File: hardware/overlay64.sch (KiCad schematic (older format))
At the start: 26 parts, among them P2 MAIN, P3 CONTROL, P6 HOLE, P7 HOLE, P8 HOLE, P9 HOLE, Q1 BC547B, U1 LM1881, Y1 20MHz

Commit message: Hardware: Updated schematics, added BURST signal connection
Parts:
- removed P3: CONTROL, Pin_Headers:Pin_Header_Angled_1x02, symbol CONN_01X02
- added P2: INPUT, symbol CONN_01X16
- added P3: CONTROL, symbol CONN_01X08
- R1, R2, R3: renamed from R?; footprint (none) -> Discret:R1
- gave numbers to parts that had none: 4
- renumbered C3 to C1, C1 to C2, C2 to C3, C5 to C4, C6 to C5, C4 to C6, P2 to P4, P6 to P5, P7 to P6, P8 to P7, P9 to P8, R2 to R4, R1 to R5
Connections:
- net labels added: C0, C1, C2, C3, C4, C5, IN0, IN1, IN10, IN11, IN12, IN13, IN14, IN15, IN2, IN3, IN4, IN5, IN6, IN7, IN8, IN9, ~BURST
- wire segments 25 -> 27
- no-connect marks 30 -> 6
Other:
- moved on the sheet: C1, C5, C6, P5, P6, P7, P8, R5

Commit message: Hardware: Added custom components, started layout
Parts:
- added P9: BYPASS, Pin_Headers:Pin_Header_Angled_1x16, symbol CONN_01X16
- D1, D2: footprint (none) -> custom:Diode-2.5mm-Vertical
- IC1: footprint DIL40 -> Housings_DIP:DIP-40_W15.24mm
- P1: footprint (none) -> custom:USB-MINI-B-TH
- P2: footprint (none) -> Pin_Headers:Pin_Header_Angled_1x16
- P3: footprint (none) -> Pin_Headers:Pin_Header_Angled_1x08
- R1, R2, R3, R4, R5: footprint Discret:R1 -> custom:R1
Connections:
- net C0: now also P3.6 (P6); no longer P3.3 (P3)
- net C1: now also P3.5 (P5); no longer P3.4 (P4)
- net C2: now also P3.4 (P4); no longer P3.5 (P5)
- net C3: now also P3.3 (P3); no longer P3.6 (P6)
- net C4: now also P3.2 (P2); no longer P3.7 (P7)
- net C5: now also P3.1 (P1); no longer P3.8 (P8)
- net D-: now also R3.1; no longer R3.2
- net IN0: now also P2.16 (P16), P9.1 (P1); no longer P2.1 (P1)
- net IN1: now also P2.15 (P15), P9.2 (P2); no longer P2.2 (P2)
- net IN10: now also IC1.27 ((PCINT21/TDI)PC5), P2.6 (P6), P9.11 (P11); no longer IC1.24 ((PCINT18/TCK)PC2), P2.11 (P11)
- net IN11: now also IC1.26 ((PCINT20/TDO)PC4), P2.5 (P5), P9.12 (P12); no longer IC1.25 ((PCINT19/TMS)PC3), P2.12 (P12)
- net IN12: now also IC1.25 ((PCINT19/TMS)PC3), P2.4 (P4), P9.13 (P13); no longer IC1.26 ((PCINT20/TDO)PC4), P2.13 (P13)
- net IN13: now also IC1.24 ((PCINT18/TCK)PC2), P2.3 (P3), P9.14 (P14); no longer IC1.27 ((PCINT21/TDI)PC5), P2.14 (P14)
- net IN14: now also IC1.23 ((PCINT17/SDA)PC1), P2.2 (P2), P9.15 (P15); no longer IC1.28 ((PCINT22/TOSC1)PC6), P2.15 (P15)
- net IN15: now also IC1.22 ((PCINT16/SCL)PC0), P2.1 (P1), P9.16 (P16); no longer IC1.29 ((PCINT23/TOSC2)PC7), P2.16 (P16)
- net IN2: now also P2.14 (P14), P9.3 (P3); no longer P2.3 (P3)
- net IN3: now also P2.13 (P13), P9.4 (P4); no longer P2.4 (P4)
- net IN4: now also P2.12 (P12), P9.5 (P5); no longer P2.5 (P5)
- net IN5: now also P2.11 (P11), P9.6 (P6); no longer P2.6 (P6)
- net IN6: now also P2.10 (P10), P9.7 (P7); no longer P2.7 (P7)
- net IN7: now also P2.9 (P9), P9.8 (P8); no longer P2.8 (P8)
- net IN8: now also IC1.29 ((PCINT23/TOSC2)PC7), P2.8 (P8), P9.9 (P9); no longer IC1.22 ((PCINT16/SCL)PC0), P2.9 (P9)
- net IN9: now also IC1.28 ((PCINT22/TOSC1)PC6), P2.7 (P7), P9.10 (P10); no longer IC1.23 ((PCINT17/SDA)PC1), P2.10 (P10)
- net VCC: now also R3.2; no longer R3.1
- net ~OE: now also P3.8 (P8); no longer P3.1 (P1)
- net ~OR: now also P3.7 (P7); no longer P3.2 (P2)
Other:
- moved on the sheet: P2, P3

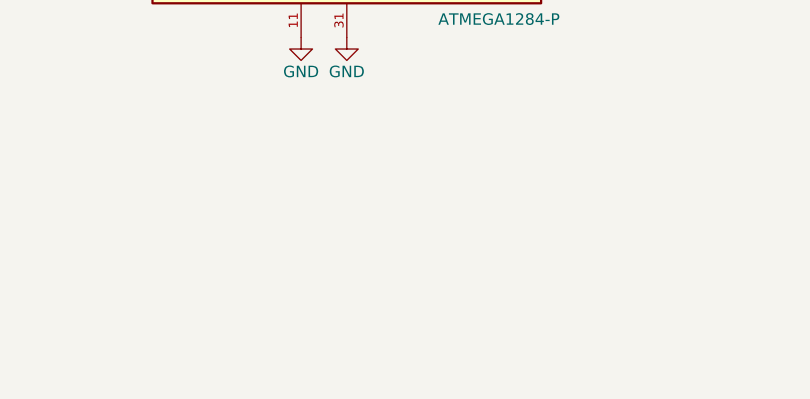
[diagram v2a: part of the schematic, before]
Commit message: Hardware: Added jumpers for manually entering the bootloader
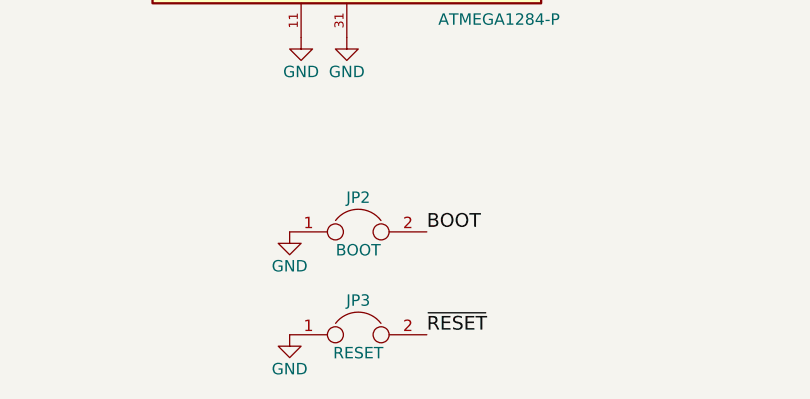
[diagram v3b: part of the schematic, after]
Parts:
- added JP2: BOOT, custom:Pin_Header_Straight_1x02_Pitch2.00mm, symbol JUMPER
- added JP3: RESET, custom:Pin_Header_Straight_1x02_Pitch2.00mm, symbol JUMPER
- JP1: footprint Pin_Headers:Pin_Header_Straight_1x02 -> custom:Pin_Header_Straight_1x02_Pitch2.00mm
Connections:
- net BOOT: now also JP2.2
- net GND: now also JP2.1, JP3.1
- net ~RESET: now also JP3.2
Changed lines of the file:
@@
 F 0 "JP1" H 7300 1750 50  0000 C CNN
 F 1 "BACKDROP" H 7300 1520 50  0000 C CNN
-F 2 "Pin_Headers:Pin_Header_Straight_1x02" H 7300 1600 50  0001 C CNN
+F 2 "custom:Pin_Header_Straight_1x02_Pitch2.00mm" H 7300 1600 50  0001 C CNN
 F 3 "" H 7300 1600 50  0000 C CNN
 	1    7300 1600
@@
 Text Label 8100 4200 0    60   ~ 0
 IN15
+$Comp
+L GND #PWR025
+U 1 1 57B5BB3D
+P 2750 6800
+F 0 "#PWR025" H 2750 6550 50  0001 C CNN
+F 1 "GND" H 2750 6650 50  0000 C CNN
+F 2 "" H 2750 6800 50  0000 C CNN
+F 3 "" H 2750 6800 50  0000 C CNN
+	1    2750 6800
+	1    0    0    -1
+$EndComp
+$Comp
+L GND #PWR026
+U 1 1 57B5BBC8
+P 2750 6350
+F 0 "#PWR026" H 2750 6100 50  0001 C CNN
+F 1 "GND" H 2750 6200 50  0000 C CNN
+F 2 "" H 2750 6350 50  0000 C CNN
+F 3 "" H 2750 6350 50  0000 C CNN
+	1    2750 6350
+	1    0    0    -1
+$EndComp
+Text Label 3350 6350 0    60   ~ 0
+BOOT
+Text Label 3350 6800 0    60   ~ 0
+~RESET
+$Comp
+L JUMPER JP2
+U 1 1 57B5CD17
+P 3050 6350
+F 0 "JP2" H 3050 6500 50  0000 C CNN
+F 1 "BOOT" H 3050 6270 50  0000 C CNN
+F 2 "custom:Pin_Header_Straight_1x02_Pitch2.00mm" H 3050 6350 50  0001 C CNN
+F 3 "" H 3050 6350 50  0000 C CNN
+	1    3050 6350
+	1    0    0    -1
+$EndComp
+$Comp
+L JUMPER JP3
+U 1 1 57B5CDC9
+P 3050 6800
+F 0 "JP3" H 3050 6950 50  0000 C CNN
+F 1 "RESET" H 3050 6720 50  0000 C CNN
+F 2 "custom:Pin_Header_Straight_1x02_Pitch2.00mm" H 3050 6800 50  0001 C CNN
+F 3 "" H 3050 6800 50  0000 C CNN
+	1    3050 6800
+	1    0    0    -1
+$EndComp
 $EndSCHEMATC

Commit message: Hardware: Prototype 2, rearranged, rerouted, added gerber files
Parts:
- D1, D2: footprint custom:Diode-2.5mm-Vertical -> custom:D3
- IC1: value ATMEGA1284-P -> ATMEGA1284
- JP1, JP2, JP3: footprint custom:Pin_Header_Straight_1x02_Pitch2.00mm -> custom:Pin_Header_Straight_1x02
- R1, R2, R3, R4, R5: footprint custom:R1 -> Discret:R3
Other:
- moved on the sheet: C4, C5, C6, JP1, P4, Q1, R4, R5, RV1, U1

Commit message: Hardware: Removed explicit OE/OR lines, relabeled control lines
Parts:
- RV1: symbol POT -> POT-RESCUE-overlay64
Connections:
- net ~OE is gone; now on net C0: IC1.20 ((PCINT30/OC2B/ICP)PD6), P3.8 (P8)
- net ~OR is gone; now on net C1: IC1.21 ((PCINT31/OC2A)PD7), P3.7 (P7)
- net C0: no longer IC1.2 ((PCINT9/CLKO/T1)PB1), P3.6 (P6)
- net C1: no longer IC1.4 ((PCINT11/AIN1/OC0)PB3), P3.5 (P5)
- net C2: now also IC1.2 ((PCINT9/CLKO/T1)PB1), P3.6 (P6); no longer IC1.7 ((PCINT14/MISO)PB6), P3.4 (P4)
- net C3: now also IC1.4 ((PCINT11/AIN1/OC0)PB3), P3.5 (P5); no longer IC1.8 ((PCINT15/SCK)PB7), P3.3 (P3)
- net C4: now also IC1.7 ((PCINT14/MISO)PB6), P3.4 (P4); no longer IC1.18 ((PCINT28/XCK1/OC1B)PD4), P3.2 (P2)
- net C5: now also IC1.8 ((PCINT15/SCK)PB7), P3.3 (P3); no longer IC1.19 ((PCINT294/OC1A)PD5), P3.1 (P1)
- new net C6: IC1.18 ((PCINT28/XCK1/OC1B)PD4), P3.2 (P2)
- new net C7: IC1.19 ((PCINT294/OC1A)PD5), P3.1 (P1)
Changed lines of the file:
@@
 EESchema Schematic File Version 2
+LIBS:overlay64-rescue
 LIBS:power
 LIBS:device
@@
 $EndComp
 $Comp
-L POT RV1
+L POT-RESCUE-overlay64 RV1
 U 1 1 56A8F98B
 P 6350 1800
@@
 $EndComp
 Text Label 4000 5200 0    60   ~ 0
-~OR
+C1
 Text Label 5400 6800 2    60   ~ 0
-~OE
+C0
 Text Label 6700 2000 0    60   ~ 0
 LUMA
@@
 $EndComp
 Text Label 4000 5100 0    60   ~ 0
-~OE
+C0
 Text Label 5400 6700 2    60   ~ 0
-~OR
+C1
 $Comp
 L CONN_01X01 P5
@@
 IN15
 Text Label 4000 2800 0    60   ~ 0
-C0
+C2
 Text Label 4000 3000 0    60   ~ 0
-C1
+C3
 Text Label 4000 3300 0    60   ~ 0
-C2
+C4
 Text Label 4000 3400 0    60   ~ 0
-C3
+C5
 Text Label 4000 4900 0    60   ~ 0
-C4
+C6
 Text Label 4000 5000 0    60   ~ 0
-C5
+C7
 $Comp
 L CONN_01X08 P3
@@
 $EndComp
 Text Label 5400 6600 2    60   ~ 0
-C0
+C2
 Text Label 5400 6500 2    60   ~ 0
-C1
+C3
 Text Label 5400 6400 2    60   ~ 0
-C2
+C4
 Text Label 5400 6300 2    60   ~ 0
-C3
+C5
 Text Label 5400 6200 2    60   ~ 0
-C4
+C6
 Text Label 5400 6100 2    60   ~ 0
-C5
+C7
 $Comp
 L GND #PWR024

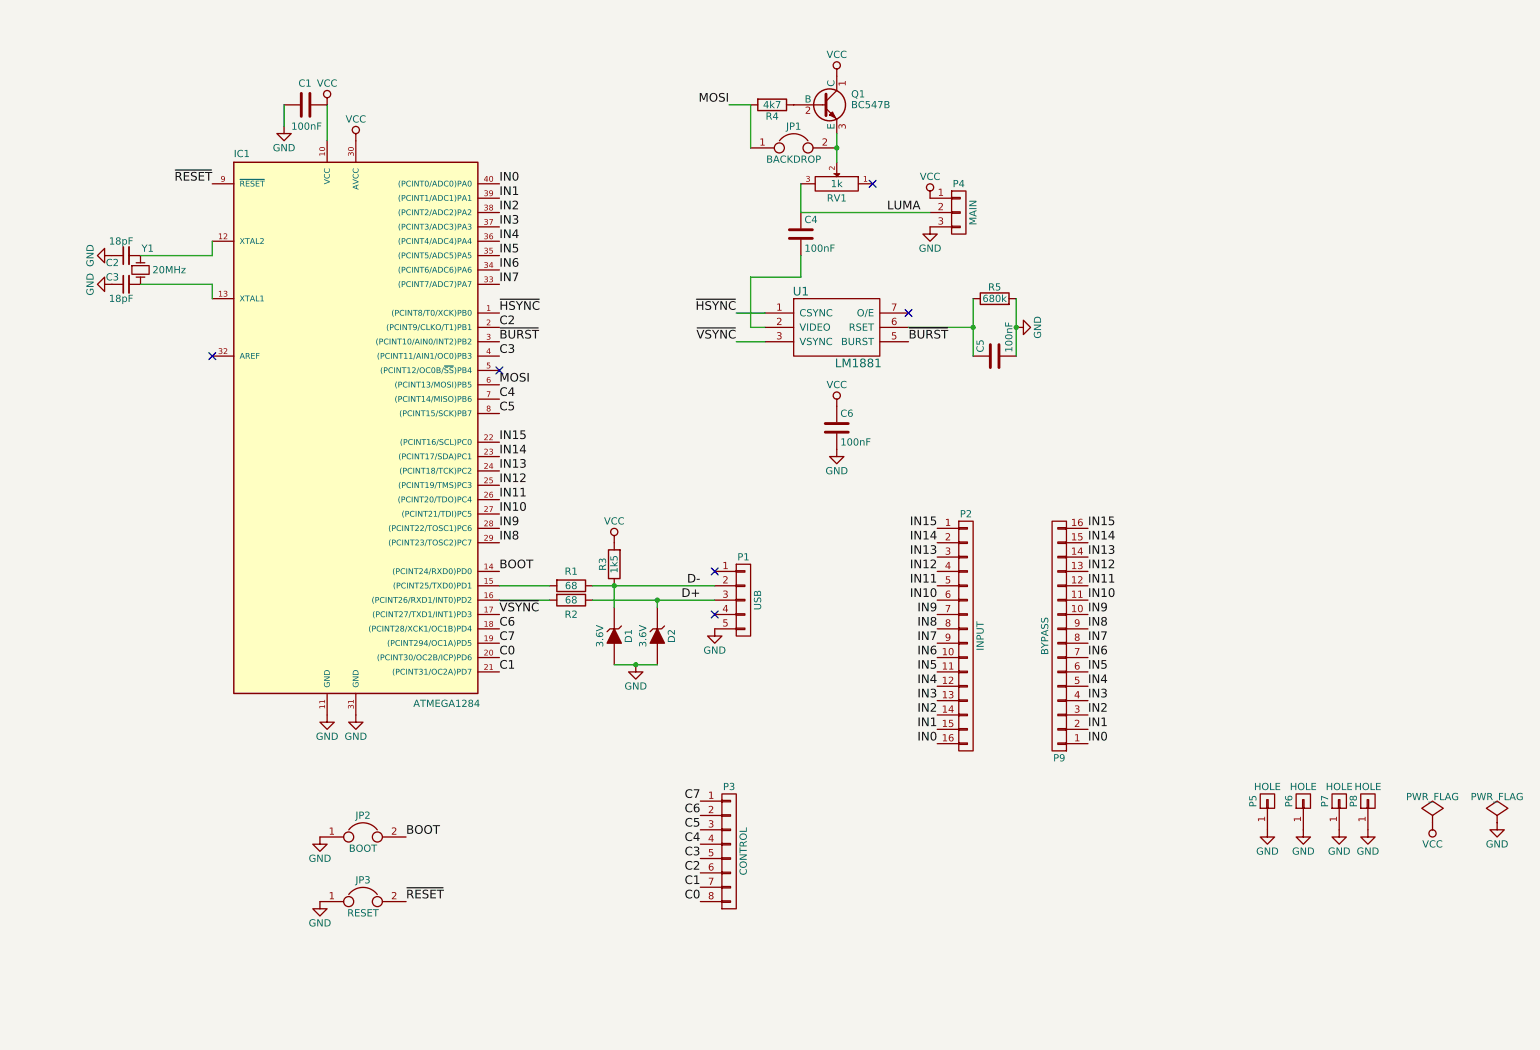
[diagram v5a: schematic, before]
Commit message: Hardware: Removed backdrop option, single boot button, rerouting...
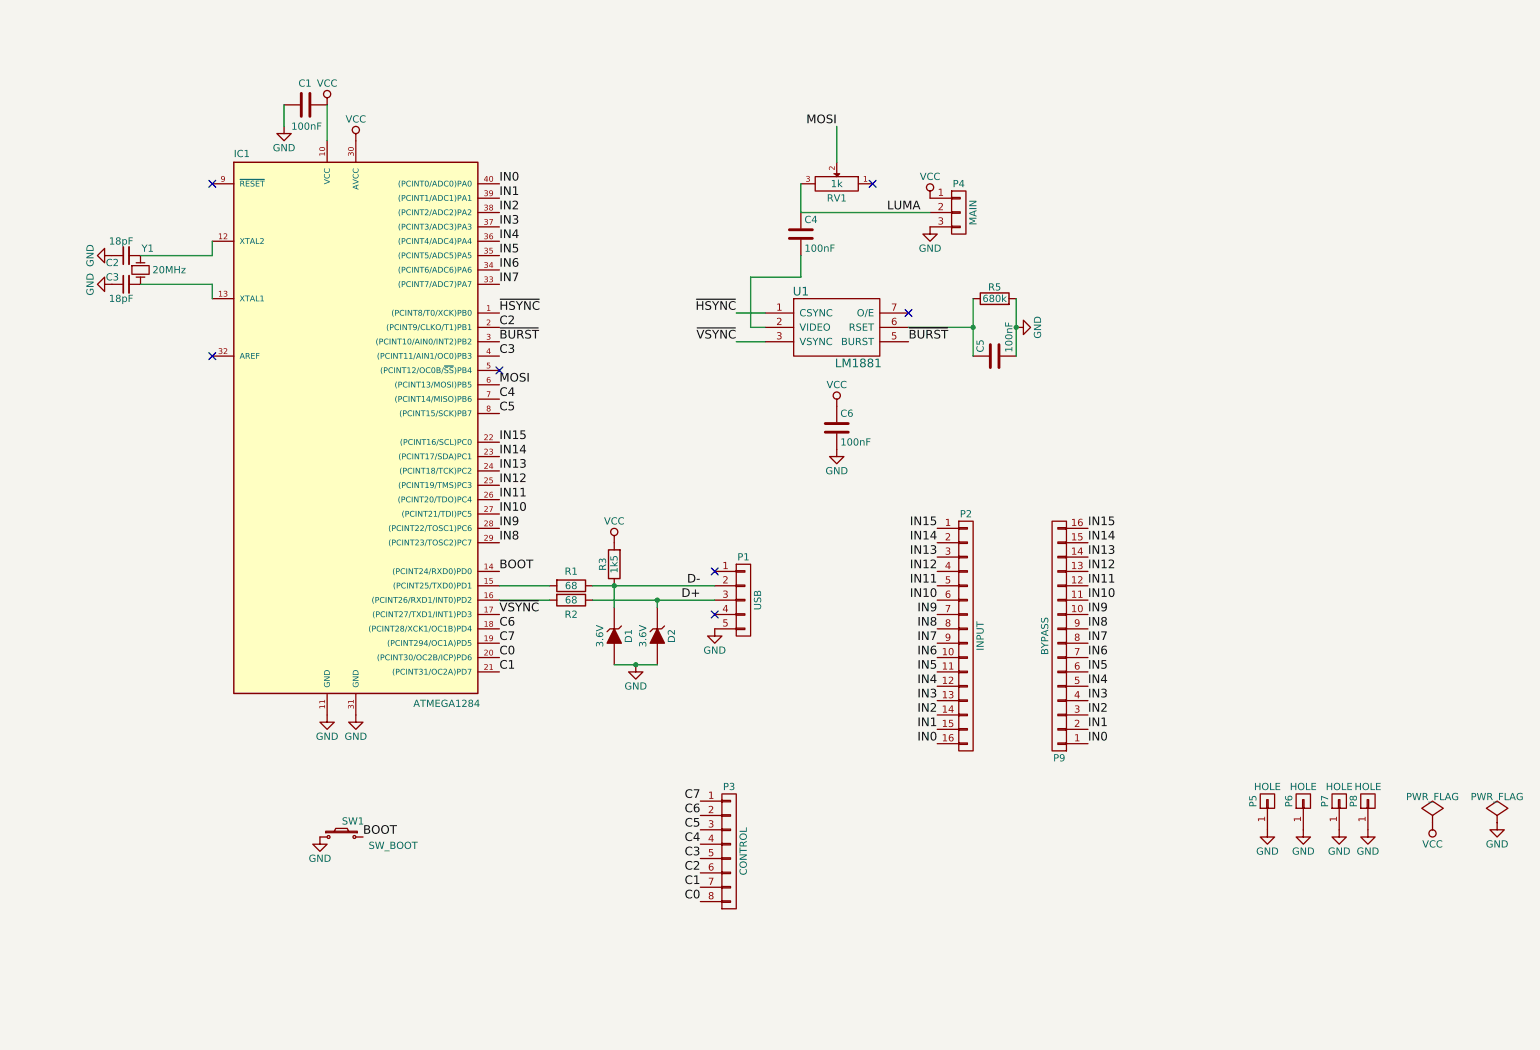
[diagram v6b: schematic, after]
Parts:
- removed JP1: BACKDROP, custom:Pin_Header_Straight_1x02, symbol JUMPER
- removed JP2: BOOT, custom:Pin_Header_Straight_1x02, symbol JUMPER
- removed JP3: RESET, custom:Pin_Header_Straight_1x02, symbol JUMPER
- removed Q1: BC547B, TO_SOT_Packages_THT:TO-92_Inline_Narrow_Oval, symbol BC547
- removed R4: 4k7, Discret:R3, symbol R
- added SW1: SW_BOOT, custom:Button, symbol SW_PUSH_SMALL_H
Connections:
- net BOOT: now also SW1.2
- net GND: now also SW1.1
- net MOSI: now also RV1.2
- net ~RESET: no longer names the net of IC1.9 (~RESET)
- no-connect marks 6 -> 7
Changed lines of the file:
@@
 Connection ~ 7600 2800
-$Comp
-L VCC #PWR09
-U 1 1 56A78618
-P 6350 1050
-F 0 "#PWR09" H 6350 900 50  0001 C CNN
-F 1 "VCC" H 6350 1200 50  0000 C CNN
-F 2 "" H 6350 1050 60  0000 C CNN
-F 3 "" H 6350 1050 60  0000 C CNN
-	1    6350 1050
-	1    0    0    -1
-$EndComp
 $Comp
 L POT-RESCUE-overlay64 RV1
@@
 $EndComp
 NoConn ~ 6600 1800
-Text Label 2000 1800 2    60   ~ 0
-~RESET
-Text Label 5600 1250 2    60   ~ 0
+Text Label 6350 1400 2    60   ~ 0
 MOSI
 $Comp
@@
 $EndComp
 $Comp
-L GND #PWR010
+L GND #PWR09
 U 1 1 56A976F1
 P 1300 2300
-F 0 "#PWR010" H 1300 2050 50  0001 C CNN
+F 0 "#PWR09" H 1300 2050 50  0001 C CNN
 F 1 "GND" H 1300 2150 50  0000 C CNN
 F 2 "" H 1300 2300 60  0000 C CNN
@@
 $EndComp
 $Comp
-L GND #PWR011
+L GND #PWR010
 U 1 1 56A97733
 P 1300 2500
-F 0 "#PWR011" H 1300 2250 50  0001 C CNN
+F 0 "#PWR010" H 1300 2250 50  0001 C CNN
 F 1 "GND" H 1300 2350 50  0000 C CNN
 F 2 "" H 1300 2500 60  0000 C CNN
@@
 $EndComp
 $Comp
-L VCC #PWR012
+L VCC #PWR011
 U 1 1 56A9E7D0
 P 7000 1900
-F 0 "#PWR012" H 7000 1750 50  0001 C CNN
+F 0 "#PWR011" H 7000 1750 50  0001 C CNN
 F 1 "VCC" H 7000 2050 50  0000 C CNN
 F 2 "" H 7000 1900 60  0000 C CNN
@@
 $EndComp
 $Comp
-L GND #PWR013
+L GND #PWR012
 U 1 1 56A9E875
 P 7000 2100
-F 0 "#PWR013" H 7000 1850 50  0001 C CNN
+F 0 "#PWR012" H 7000 1850 50  0001 C CNN
 F 1 "GND" H 7000 1950 50  0000 C CNN
 F 2 "" H 7000 2100 60  0000 C CNN
@@
 Wire Wire Line
 	5750 2800 5750 2450
-$Comp
-L R R4
-U 1 1 56AA9AFF
-P 5900 1250
-F 0 "R4" V 5980 1250 50  0000 C CNN
-F 1 "4k7" V 5900 1250 50  0000 C CNN
-F 2 "Discret:R3" V 5830 1250 50  0001 C CNN
-F 3 "" H 5900 1250 50  0000 C CNN
-	1    5900 1250
-	0    1    1    0
-$EndComp
 Text Label 4000 5200 0    60   ~ 0
 C1
@@
 Text Label 6700 2000 0    60   ~ 0
 LUMA
-$Comp
-L JUMPER JP1
-U 1 1 56B2539D
-P 6050 1550
-F 0 "JP1" H 6050 1700 50  0000 C CNN
-F 1 "BACKDROP" H 6050 1470 50  0000 C CNN
-F 2 "custom:Pin_Header_Straight_1x02" H 6050 1550 50  0001 C CNN
-F 3 "" H 6050 1550 50  0000 C CNN
-	1    6050 1550
-	1    0    0    -1
-$EndComp
-Wire Wire Line
-	6350 1450 6350 1650
-Connection ~ 6350 1550
 Wire Wire Line
 	6100 1800 6100 2000
-Wire Wire Line
-	5750 1250 5750 1550
-$Comp
-L BC547 Q1
-U 1 1 56B5F1A8
-P 6250 1250
-F 0 "Q1" H 6450 1325 50  0000 L CNN
-F 1 "BC547B" H 6450 1250 50  0000 L CNN
-F 2 "TO_SOT_Packages_THT:TO-92_Inline_Narrow_Oval" H 6450 1175 50  0001 L CIN
-F 3 "" H 6250 1250 50  0000 L CNN
-	1    6250 1250
-	1    0    0    -1
-$EndComp
 Text Label 4000 5100 0    60   ~ 0
 C0
@@
 $EndComp
 $Comp
-L GND #PWR014
+L GND #PWR013
 U 1 1 57445C4B
 P 9350 6300
-F 0 "#PWR014" H 9350 6050 50  0001 C CNN
+F 0 "#PWR013" H 9350 6050 50  0001 C CNN
 F 1 "GND" H 9350 6150 50  0000 C CNN
 F 2 "" H 9350 6300 60  0000 C CNN
@@
 $EndComp
 $Comp
-L GND #PWR015
+L GND #PWR014
 U 1 1 57445CA2
 P 9600 6300
-F 0 "#PWR015" H 9600 6050 50  0001 C CNN
+F 0 "#PWR014" H 9600 6050 50  0001 C CNN
 F 1 "GND" H 9600 6150 50  0000 C CNN
 F 2 "" H 9600 6300 60  0000 C CNN
@@
 $EndComp
 $Comp
-L GND #PWR016
+L GND #PWR015
 U 1 1 57445CF2
 P 9850 6300
-F 0 "#PWR016" H 9850 6050 50  0001 C CNN
+F 0 "#PWR015" H 9850 6050 50  0001 C CNN
 F 1 "GND" H 9850 6150 50  0000 C CNN
 F 2 "" H 9850 6300 60  0000 C CNN
@@
 $EndComp
 $Comp
-L GND #PWR017
+L GND #PWR016
 U 1 1 57445D42
 P 10050 6300
-F 0 "#PWR017" H 10050 6050 50  0001 C CNN
+F 0 "#PWR016" H 10050 6050 50  0001 C CNN
 F 1 "GND" H 10050 6150 50  0000 C CNN
 F 2 "" H 10050 6300 60  0000 C CNN
@@
 	2000 2300 2000 2200
 $Comp
-L VCC #PWR018
+L VCC #PWR017
 U 1 1 5799D81B
 P 3000 1500
-F 0 "#PWR018" H 3000 1350 50  0001 C CNN
+F 0 "#PWR017" H 3000 1350 50  0001 C CNN
 F 1 "VCC" H 3000 1650 50  0000 C CNN
 F 2 "" H 3000 1500 60  0000 C CNN
@@
 NoConn ~ 2000 3000
 $Comp
-L GND #PWR019
+L GND #PWR018
 U 1 1 5799D944
 P 2800 5500
-F 0 "#PWR019" H 2800 5250 50  0001 C CNN
+F 0 "#PWR018" H 2800 5250 50  0001 C CNN
 F 1 "GND" H 2800 5350 50  0000 C CNN
 F 2 "" H 2800 5500 50  0000 C CNN
@@
 $EndComp
 $Comp
-L GND #PWR020
+L GND #PWR019
 U 1 1 5799DAD2
 P 3000 5500
-F 0 "#PWR020" H 3000 5250 50  0001 C CNN
+F 0 "#PWR019" H 3000 5250 50  0001 C CNN
 F 1 "GND" H 3000 5350 50  0000 C CNN
 F 2 "" H 3000 5500 50  0000 C CNN
@@
 Text Label 5650 2700 2    60   ~ 0
 ~HSYNC
-Wire Wire Line
-	5750 1250 5600 1250
 Text Label 5650 2900 2    60   ~ 0
 ~VSYNC
@@
 $EndComp
 $Comp
-L VCC #PWR021
+L VCC #PWR020
 U 1 1 5799FB47
 P 4800 4300
-F 0 "#PWR021" H 4800 4150 50  0001 C CNN
+F 0 "#PWR020" H 4800 4150 50  0001 C CNN
 F 1 "VCC" H 4800 4450 50  0000 C CNN
 F 2 "" H 4800 4300 50  0000 C CNN
@@
 $EndComp
 $Comp
-L GND #PWR022
+L GND #PWR021
 U 1 1 579A0108
 P 4950 5150
-F 0 "#PWR022" H 4950 4900 50  0001 C CNN
+F 0 "#PWR021" H 4950 4900 50  0001 C CNN
 F 1 "GND" H 4950 5000 50  0000 C CNN
 F 2 "" H 4950 5150 50  0000 C CNN
@@
 NoConn ~ 5500 4800
 $Comp
-L GND #PWR023
+L GND #PWR022
 U 1 1 579A190A
 P 5500 4900
-F 0 "#PWR023" H 5500 4650 50  0001 C CNN
+F 0 "#PWR022" H 5500 4650 50  0001 C CNN
 F 1 "GND" H 5500 4750 50  0000 C CNN
 F 2 "" H 5500 4900 50  0000 C CNN
@@
 C7
 $Comp
-L GND #PWR024
+L GND #PWR023
 U 1 1 57A1101A
 P 2500 1400
-F 0 "#PWR024" H 2500 1150 50  0001 C CNN
+F 0 "#PWR023" H 2500 1150 50  0001 C CNN
 F 1 "GND" H 2500 1250 50  0000 C CNN
 F 2 "" H 2500 1400 50  0000 C CNN
@@
 IN15
 $Comp
-L GND #PWR025
-U 1 1 57B5BB3D
-P 2750 6800
-F 0 "#PWR025" H 2750 6550 50  0001 C CNN
-F 1 "GND" H 2750 6650 50  0000 C CNN
-F 2 "" H 2750 6800 50  0000 C CNN
-F 3 "" H 2750 6800 50  0000 C CNN
-	1    2750 6800
-	1    0    0    -1
-$EndComp
-$Comp
-L GND #PWR026
+L GND #PWR024
 U 1 1 57B5BBC8
 P 2750 6350
-F 0 "#PWR026" H 2750 6100 50  0001 C CNN
+F 0 "#PWR024" H 2750 6100 50  0001 C CNN
 F 1 "GND" H 2750 6200 50  0000 C CNN
 F 2 "" H 2750 6350 50  0000 C CNN
@@
 	1    0    0    -1
 $EndComp
-Text Label 3350 6350 0    60   ~ 0
+Text Label 3050 6350 0    60   ~ 0
 BOOT
-Text Label 3350 6800 0    60   ~ 0
-~RESET
-$Comp
-L JUMPER JP2
-U 1 1 57B5CD17
-P 3050 6350
-F 0 "JP2" H 3050 6500 50  0000 C CNN
-F 1 "BOOT" H 3050 6270 50  0000 C CNN
-F 2 "custom:Pin_Header_Straight_1x02" H 3050 6350 50  0001 C CNN
-F 3 "" H 3050 6350 50  0000 C CNN
-	1    3050 6350
-	1    0    0    -1
-$EndComp
-$Comp
-L JUMPER JP3
-U 1 1 57B5CDC9
-P 3050 6800
-F 0 "JP3" H 3050 6950 50  0000 C CNN
-F 1 "RESET" H 3050 6720 50  0000 C CNN
-F 2 "custom:Pin_Header_Straight_1x02" H 3050 6800 50  0001 C CNN
-F 3 "" H 3050 6800 50  0000 C CNN
-	1    3050 6800
-	1    0    0    -1
-$EndComp
+NoConn ~ 2000 1800
+Wire Wire Line
+	6350 1650 6350 1400
+$Comp
+L SW_PUSH_SMALL_H SW1
+U 1 1 5832A426
+P 2900 6350
+F 0 "SW1" H 2980 6460 50  0000 C CNN
+F 1 "SW_BOOT" H 3260 6290 50  0000 C CNN
+F 2 "custom:Button" H 2900 6550 50  0001 C CNN
+F 3 "" H 2900 6550 50  0000 C CNN
+	1    2900 6350
+	1    0    0    -1
+$EndComp
